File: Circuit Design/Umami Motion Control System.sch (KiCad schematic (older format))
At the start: 7 parts

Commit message: schematic work
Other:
- moved on the sheet: C?, IC?, K?, X?
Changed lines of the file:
@@
 $Descr A4 11693 8268
 encoding utf-8
-Sheet 1 2
+Sheet 1 3
 Title ""
 Date "8 may 2014"
@@
 L ATMEGA328P-P-RESCUE-Umami_Motion_Control_System IC?
 U 1 1 53642346
-P 4700 3900
-F 0 "IC?" H 3950 5150 40  0000 L BNN
-F 1 "ATMEGA328P-P" H 5100 2500 40  0000 L BNN
-F 2 "DIL28" H 4700 3900 30  0000 C CIN
-F 3 "" H 4700 3900 60  0000 C CNN
-	1    4700 3900
+P 13650 4150
+F 0 "IC?" H 12900 5400 40  0000 L BNN
+F 1 "ATMEGA328P-P" H 14050 2750 40  0000 L BNN
+F 2 "DIL28" H 13650 4150 30  0000 C CIN
+F 3 "" H 13650 4150 60  0000 C CNN
+	1    13650 4150
 	1    0    0    -1
 $EndComp
@@
 L CONN_3 K?
 U 1 1 536423A1
-P 7250 1900
-F 0 "K?" V 7200 1900 50  0000 C CNN
-F 1 "CONN_3" V 7300 1900 40  0000 C CNN
-F 2 "" H 7250 1900 60  0000 C CNN
-F 3 "" H 7250 1900 60  0000 C CNN
-	1    7250 1900
+P 16200 2150
+F 0 "K?" V 16150 2150 50  0000 C CNN
+F 1 "CONN_3" V 16250 2150 40  0000 C CNN
+F 2 "" H 16200 2150 60  0000 C CNN
+F 3 "" H 16200 2150 60  0000 C CNN
+	1    16200 2150
 	1    0    0    -1
 $EndComp
@@
 L CRYSTAL X?
 U 1 1 5364240B
-P 7650 3450
-F 0 "X?" H 7650 3600 60  0000 C CNN
-F 1 "CRYSTAL" H 7650 3300 60  0000 C CNN
-F 2 "~" H 7650 3450 60  0000 C CNN
-F 3 "~" H 7650 3450 60  0000 C CNN
-	1    7650 3450
+P 16600 3700
+F 0 "X?" H 16600 3850 60  0000 C CNN
+F 1 "CRYSTAL" H 16600 3550 60  0000 C CNN
+F 2 "~" H 16600 3700 60  0000 C CNN
+F 3 "~" H 16600 3700 60  0000 C CNN
+	1    16600 3700
 	0    1    1    0
 $EndComp
-Text Notes 7400 1800 0    60   ~ 0
+Text Notes 16350 2050 0    60   ~ 0
 pan pot
 $Comp
 L CONN_3 K?
 U 1 1 53642559
-P 7250 2300
-F 0 "K?" V 7200 2300 50  0000 C CNN
-F 1 "CONN_3" V 7300 2300 40  0000 C CNN
-F 2 "" H 7250 2300 60  0000 C CNN
-F 3 "" H 7250 2300 60  0000 C CNN
-	1    7250 2300
+P 16200 2550
+F 0 "K?" V 16150 2550 50  0000 C CNN
+F 1 "CONN_3" V 16250 2550 40  0000 C CNN
+F 2 "" H 16200 2550 60  0000 C CNN
+F 3 "" H 16200 2550 60  0000 C CNN
+	1    16200 2550
 	1    0    0    -1
 $EndComp
-Text Notes 7400 2200 0    60   ~ 0
+Text Notes 16350 2450 0    60   ~ 0
 tilt pot
 $Comp
 L +5V #PWR?
 U 1 1 53642590
-P 4450 1400
-F 0 "#PWR?" H 4450 1490 20  0001 C CNN
-F 1 "+5V" H 4450 1550 30  0000 C CNN
-F 2 "" H 4450 1400 60  0000 C CNN
-F 3 "" H 4450 1400 60  0000 C CNN
-	1    4450 1400
+P 13400 1650
+F 0 "#PWR?" H 13400 1740 20  0001 C CNN
+F 1 "+5V" H 13400 1800 30  0000 C CNN
+F 2 "" H 13400 1650 60  0000 C CNN
+F 3 "" H 13400 1650 60  0000 C CNN
+	1    13400 1650
 	1    0    0    -1
 $EndComp
-Text Notes 7400 2550 0    60   ~ 0
+Text Notes 16350 2800 0    60   ~ 0
 Focus Pot
 $Comp
 L C-RESCUE-Umami_Motion_Control_System C?
 U 1 1 536C0691
-P 7850 3750
-F 0 "C?" H 7850 3850 40  0000 L CNN
-F 1 "C" H 7856 3665 40  0000 L CNN
-F 2 "~" H 7888 3600 30  0000 C CNN
-F 3 "~" H 7850 3750 60  0000 C CNN
-	1    7850 3750
+P 16800 4000
+F 0 "C?" H 16800 4100 40  0000 L CNN
+F 1 "C" H 16806 3915 40  0000 L CNN
+F 2 "~" H 16838 3850 30  0000 C CNN
+F 3 "~" H 16800 4000 60  0000 C CNN
+	1    16800 4000
 	0    -1   -1   0
 $EndComp
@@
 L C-RESCUE-Umami_Motion_Control_System C?
 U 1 1 536C06A8
-P 7850 3150
-F 0 "C?" H 7850 3250 40  0000 L CNN
-F 1 "C" H 7856 3065 40  0000 L CNN
-F 2 "~" H 7888 3000 30  0000 C CNN
-F 3 "~" H 7850 3150 60  0000 C CNN
-	1    7850 3150
+P 16800 3400
+F 0 "C?" H 16800 3500 40  0000 L CNN
+F 1 "C" H 16806 3315 40  0000 L CNN
+F 2 "~" H 16838 3250 30  0000 C CNN
+F 3 "~" H 16800 3400 60  0000 C CNN
+	1    16800 3400
 	0    -1   -1   0
 $EndComp
@@
 L CONN_3 K?
 U 1 1 5364264D
-P 7250 2650
-F 0 "K?" V 7200 2650 50  0000 C CNN
-F 1 "CONN_3" V 7300 2650 40  0000 C CNN
-F 2 "" H 7250 2650 60  0000 C CNN
-F 3 "" H 7250 2650 60  0000 C CNN
-	1    7250 2650
+P 16200 2900
+F 0 "K?" V 16150 2900 50  0000 C CNN
+F 1 "CONN_3" V 16250 2900 40  0000 C CNN
+F 2 "" H 16200 2900 60  0000 C CNN
+F 3 "" H 16200 2900 60  0000 C CNN
+	1    16200 2900
 	1    0    0    -1
 $EndComp
@@
 L GND-RESCUE-Umami_Motion_Control_System #PWR?
 U 1 1 536C0735
-P 8050 5250
-F 0 "#PWR?" H 8050 5250 30  0001 C CNN
-F 1 "GND" H 8050 5180 30  0001 C CNN
-F 2 "" H 8050 5250 60  0000 C CNN
-F 3 "" H 8050 5250 60  0000 C CNN
-	1    8050 5250
+P 17000 5500
+F 0 "#PWR?" H 17000 5500 30  0001 C CNN
+F 1 "GND" H 17000 5430 30  0001 C CNN
+F 2 "" H 17000 5500 60  0000 C CNN
+F 3 "" H 17000 5500 60  0000 C CNN
+	1    17000 5500
 	1    0    0    -1
 $EndComp
 Wire Wire Line
-	6300 3850 5700 3850
+	15250 4100 14650 4100
 Wire Wire Line
-	6300 2650 6300 3850
+	15250 2900 15250 4100
 Wire Wire Line
-	6900 2650 6300 2650
+	15850 2900 15250 2900
 Wire Wire Line
-	6250 3750 5700 3750
+	15200 4000 14650 4000
 Wire Wire Line
-	6250 2300 6250 3750
+	15200 2550 15200 4000
 Wire Wire Line
-	6900 2300 6250 2300
+	15850 2550 15200 2550
 Wire Wire Line
-	6200 3650 5700 3650
+	15150 3900 14650 3900
 Wire Wire Line
-	6200 1900 6200 3650
+	15150 2150 15150 3900
 Wire Wire Line
-	6900 1900 6200 1900
-Connection ~ 4450 1800
+	15850 2150 15150 2150
+Connection ~ 13400 2050
 Wire Wire Line
-	4450 2200 6900 2200
+	13400 2450 15850 2450
 Wire Wire Line
-	4450 1400 4450 2550
+	13400 1650 13400 2800
 Wire Wire Line
-	5700 3500 7400 3500
+	14650 3750 16350 3750
 Wire Wire Line
-	5700 3400 7400 3400
+	14650 3650 16350 3650
 Wire Wire Line
-	7400 3400 7400 3150
+	16350 3650 16350 3400
 Wire Wire Line
-	7400 3150 7650 3150
+	16350 3400 16600 3400
 Wire Wire Line
-	7400 3500 7400 3750
+	16350 3750 16350 4000
 Wire Wire Line
-	7400 3750 7650 3750
+	16350 4000 16600 4000
 Wire Wire Line
-	8050 2900 8050 3750
+	17000 3150 17000 4000
 Wire Wire Line
-	8050 3800 8050 5250
+	17000 4050 17000 5500
 Wire Wire Line
-	6900 2000 6700 2000
+	15850 2250 15650 2250
 Wire Wire Line
-	6700 2000 6700 2900
+	15650 2250 15650 3150
 Wire Wire Line
-	6700 2900 8050 2900
-Connection ~ 8050 3150
+	15650 3150 17000 3150
+Connection ~ 17000 3400
 Wire Wire Line
-	6900 2400 6700 2400
-Connection ~ 6700 2400
+	15850 2650 15650 2650
+Connection ~ 15650 2650
 Wire Wire Line
-	6900 2750 6700 2750
-Connection ~ 6700 2750
+	15850 3000 15650 3000
+Connection ~ 15650 3000
 Wire Wire Line
-	3800 1800 6900 1800
+	12750 2050 15850 2050
 Wire Wire Line
-	4450 2550 6900 2550
-Connection ~ 4450 2200
+	13400 2800 15850 2800
+Connection ~ 13400 2450
 Wire Wire Line
-	3800 1800 3800 2800
+	12750 2050 12750 3050
 $Sheet
 S 1250 1100 900  550
@@
 F1 "Raspi.sch" 60
 $EndSheet
+$Sheet
+S 1200 2900 1150 1150
+U 565B4BE2
+F0 "old work" 60
+F1 "oldwork.sch" 60
+$EndSheet
 $EndSCHEMATC

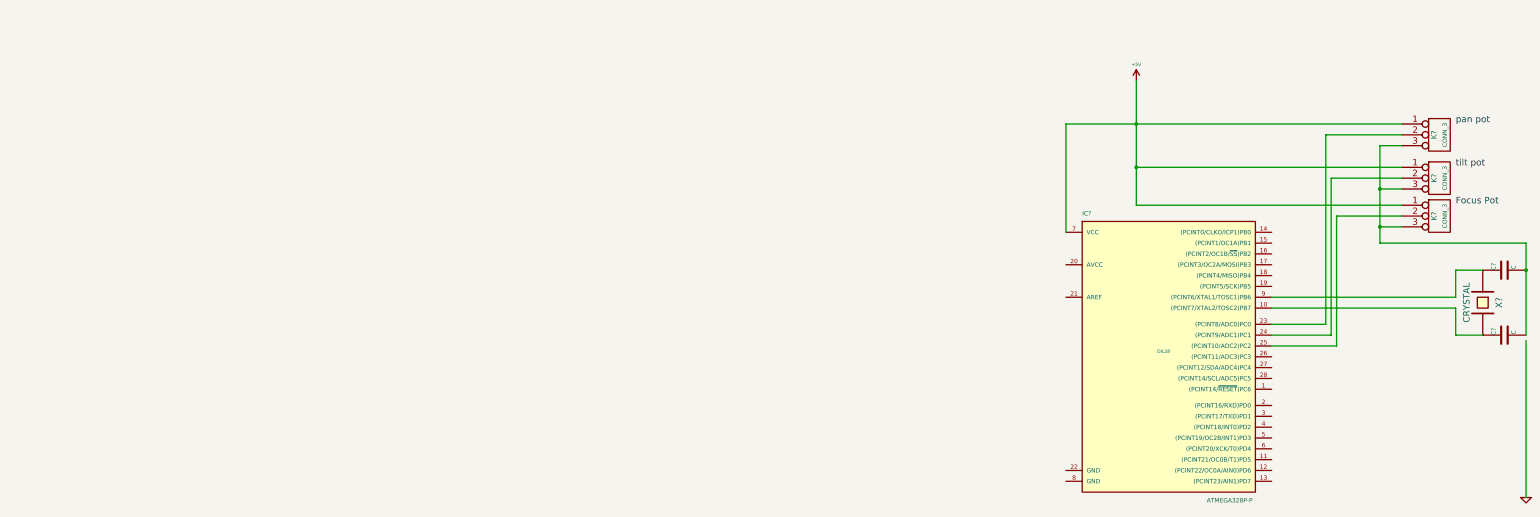
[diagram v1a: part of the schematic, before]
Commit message: socket io working, able to toggle led with phone
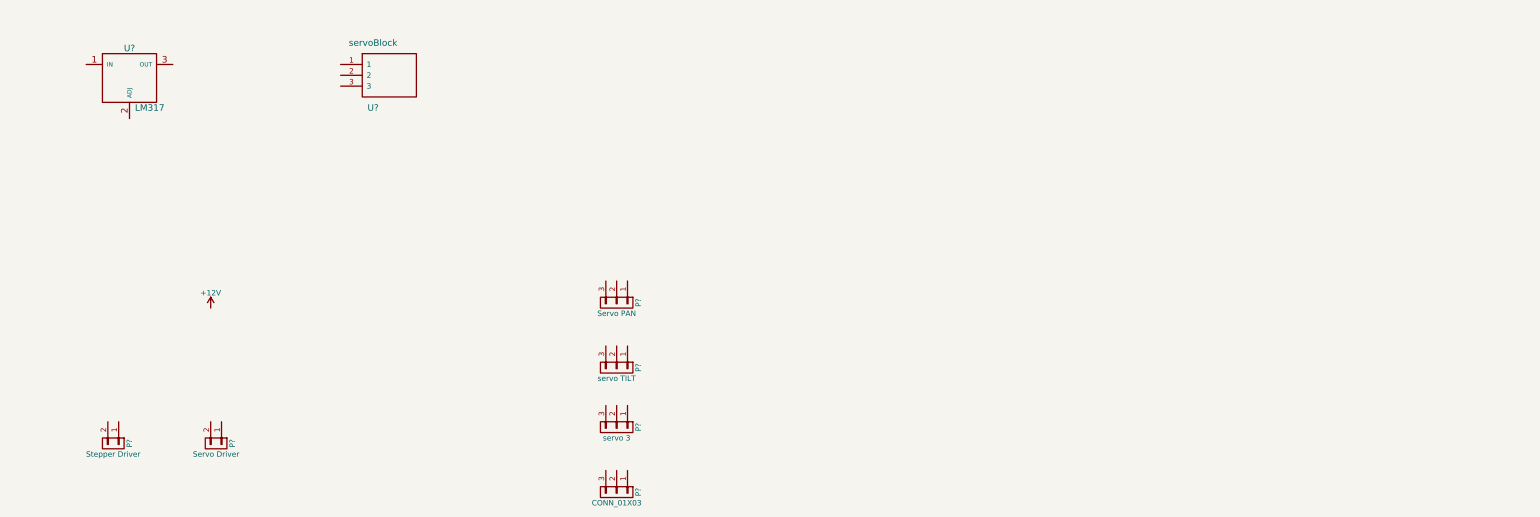
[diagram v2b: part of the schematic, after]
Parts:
- removed C? (x2): C, ~, symbol C-RESCUE-Umami_Motion_Control_System
- removed IC?: ATMEGA328P-P, DIL28, symbol ATMEGA328P-P-RESCUE-Umami_Motion_Control_System
- removed K? (x3): CONN_3, symbol CONN_3
- removed X?: CRYSTAL, ~, symbol CRYSTAL
- added P?: Servo PAN, symbol CONN_01X03
- added P?: servo TILT, symbol CONN_01X03
- added P?: servo 3, symbol CONN_01X03
- added P?: CONN_01X03, symbol CONN_01X03
- added P?: Servo Driver, symbol CONN_01X02
- added P?: Stepper Driver, symbol CONN_01X02
- added U?: LM317, symbol LM317
- added U?: servoBlock, symbol servoBlock
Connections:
- net labels added: +12V
- net labels removed: +5V, GND
- wire segments 27 -> 0
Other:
- note removed: "Focus Pot"
- note removed: "pan pot"
- note removed: "tilt pot"
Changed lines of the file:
@@
 Comment4 ""
 $EndDescr
-$Comp
-L ATMEGA328P-P-RESCUE-Umami_Motion_Control_System IC?
-U 1 1 53642346
-P 13650 4150
-F 0 "IC?" H 12900 5400 40  0000 L BNN
-F 1 "ATMEGA328P-P" H 14050 2750 40  0000 L BNN
-F 2 "DIL28" H 13650 4150 30  0000 C CIN
-F 3 "" H 13650 4150 60  0000 C CNN
-	1    13650 4150
-	1    0    0    -1
-$EndComp
-$Comp
-L CONN_3 K?
-U 1 1 536423A1
-P 16200 2150
-F 0 "K?" V 16150 2150 50  0000 C CNN
-F 1 "CONN_3" V 16250 2150 40  0000 C CNN
-F 2 "" H 16200 2150 60  0000 C CNN
-F 3 "" H 16200 2150 60  0000 C CNN
-	1    16200 2150
-	1    0    0    -1
-$EndComp
-$Comp
-L CRYSTAL X?
-U 1 1 5364240B
-P 16600 3700
-F 0 "X?" H 16600 3850 60  0000 C CNN
-F 1 "CRYSTAL" H 16600 3550 60  0000 C CNN
-F 2 "~" H 16600 3700 60  0000 C CNN
-F 3 "~" H 16600 3700 60  0000 C CNN
-	1    16600 3700
-	0    1    1    0
-$EndComp
-Text Notes 16350 2050 0    60   ~ 0
-pan pot
-$Comp
-L CONN_3 K?
-U 1 1 53642559
-P 16200 2550
-F 0 "K?" V 16150 2550 50  0000 C CNN
-F 1 "CONN_3" V 16250 2550 40  0000 C CNN
-F 2 "" H 16200 2550 60  0000 C CNN
-F 3 "" H 16200 2550 60  0000 C CNN
-	1    16200 2550
-	1    0    0    -1
-$EndComp
-Text Notes 16350 2450 0    60   ~ 0
-tilt pot
-$Comp
-L +5V #PWR?
-U 1 1 53642590
-P 13400 1650
-F 0 "#PWR?" H 13400 1740 20  0001 C CNN
-F 1 "+5V" H 13400 1800 30  0000 C CNN
-F 2 "" H 13400 1650 60  0000 C CNN
-F 3 "" H 13400 1650 60  0000 C CNN
-	1    13400 1650
-	1    0    0    -1
-$EndComp
-Text Notes 16350 2800 0    60   ~ 0
-Focus Pot
-$Comp
-L C-RESCUE-Umami_Motion_Control_System C?
-U 1 1 536C0691
-P 16800 4000
-F 0 "C?" H 16800 4100 40  0000 L CNN
-F 1 "C" H 16806 3915 40  0000 L CNN
-F 2 "~" H 16838 3850 30  0000 C CNN
-F 3 "~" H 16800 4000 60  0000 C CNN
-	1    16800 4000
-	0    -1   -1   0
-$EndComp
-$Comp
-L C-RESCUE-Umami_Motion_Control_System C?
-U 1 1 536C06A8
-P 16800 3400
-F 0 "C?" H 16800 3500 40  0000 L CNN
-F 1 "C" H 16806 3315 40  0000 L CNN
-F 2 "~" H 16838 3250 30  0000 C CNN
-F 3 "~" H 16800 3400 60  0000 C CNN
-	1    16800 3400
-	0    -1   -1   0
-$EndComp
-$Comp
-L CONN_3 K?
-U 1 1 5364264D
-P 16200 2900
-F 0 "K?" V 16150 2900 50  0000 C CNN
-F 1 "CONN_3" V 16250 2900 40  0000 C CNN
-F 2 "" H 16200 2900 60  0000 C CNN
-F 3 "" H 16200 2900 60  0000 C CNN
-	1    16200 2900
-	1    0    0    -1
-$EndComp
-$Comp
-L GND-RESCUE-Umami_Motion_Control_System #PWR?
-U 1 1 536C0735
-P 17000 5500
-F 0 "#PWR?" H 17000 5500 30  0001 C CNN
-F 1 "GND" H 17000 5430 30  0001 C CNN
-F 2 "" H 17000 5500 60  0000 C CNN
-F 3 "" H 17000 5500 60  0000 C CNN
-	1    17000 5500
-	1    0    0    -1
-$EndComp
-Wire Wire Line
-	15250 4100 14650 4100
-Wire Wire Line
-	15250 2900 15250 4100
-Wire Wire Line
-	15850 2900 15250 2900
-Wire Wire Line
-	15200 4000 14650 4000
-Wire Wire Line
-	15200 2550 15200 4000
-Wire Wire Line
-	15850 2550 15200 2550
-Wire Wire Line
-	15150 3900 14650 3900
-Wire Wire Line
-	15150 2150 15150 3900
-Wire Wire Line
-	15850 2150 15150 2150
-Connection ~ 13400 2050
-Wire Wire Line
-	13400 2450 15850 2450
-Wire Wire Line
-	13400 1650 13400 2800
-Wire Wire Line
-	14650 3750 16350 3750
-Wire Wire Line
-	14650 3650 16350 3650
-Wire Wire Line
-	16350 3650 16350 3400
-Wire Wire Line
-	16350 3400 16600 3400
-Wire Wire Line
-	16350 3750 16350 4000
-Wire Wire Line
-	16350 4000 16600 4000
-Wire Wire Line
-	17000 3150 17000 4000
-Wire Wire Line
-	17000 4050 17000 5500
-Wire Wire Line
-	15850 2250 15650 2250
-Wire Wire Line
-	15650 2250 15650 3150
-Wire Wire Line
-	15650 3150 17000 3150
-Connection ~ 17000 3400
-Wire Wire Line
-	15850 2650 15650 2650
-Connection ~ 15650 2650
-Wire Wire Line
-	15850 3000 15650 3000
-Connection ~ 15650 3000
-Wire Wire Line
-	12750 2050 15850 2050
-Wire Wire Line
-	13400 2800 15850 2800
-Connection ~ 13400 2450
-Wire Wire Line
-	12750 2050 12750 3050
 $Sheet
 S 1250 1100 900  550
@@
 F1 "oldwork.sch" 60
 $EndSheet
+$Comp
+L LM317 U?
+U 1 1 565B5C82
+P 4100 1650
+F 0 "U?" H 4100 1950 60  0000 C CNN
+F 1 "LM317" H 4150 1400 60  0000 L CNN
+F 2 "" H 4100 1650 60  0000 C CNN
+F 3 "" H 4100 1650 60  0000 C CNN
+	1    4100 1650
+	1    0    0    -1
+$EndComp
+$Comp
+L servoBlock U?
+U 1 1 565B76FD
+P 6350 1400
+F 0 "U?" H 6350 900 60  0000 C CNN
+F 1 "servoBlock" H 6350 1500 60  0000 C CNN
+F 2 "" H 6050 1400 60  0000 C CNN
+F 3 "" H 6050 1400 60  0000 C CNN
+	1    6350 1400
+	1    0    0    -1
+$EndComp
+$Comp
+L CONN_01X03 P?
+U 1 1 565B7937
+P 8600 3700
+F 0 "P?" H 8600 3900 50  0000 C CNN
+F 1 "Servo PAN" V 8700 3700 50  0000 C CNN
+F 2 "" H 8600 3700 60  0000 C CNN
+F 3 "" H 8600 3700 60  0000 C CNN
+	1    8600 3700
+	0    1    1    0
+$EndComp
+$Comp
+L CONN_01X03 P?
+U 1 1 565B79D8
+P 8600 4300
+F 0 "P?" H 8600 4500 50  0000 C CNN
+F 1 "servo TILT" V 8700 4300 50  0000 C CNN
+F 2 "" H 8600 4300 60  0000 C CNN
+F 3 "" H 8600 4300 60  0000 C CNN
+	1    8600 4300
+	0    1    1    0
+$EndComp
+$Comp
+L CONN_01X03 P?
+U 1 1 565B7A79
+P 8600 4850
+F 0 "P?" H 8600 5050 50  0000 C CNN
+F 1 "servo 3" V 8700 4850 50  0000 C CNN
+F 2 "" H 8600 4850 60  0000 C CNN
+F 3 "" H 8600 4850 60  0000 C CNN
+	1    8600 4850
+	0    1    1    0
+$EndComp
+$Comp
+L CONN_01X03 P?
+U 1 1 565B7AAE
+P 8600 5450
+F 0 "P?" H 8600 5650 50  0000 C CNN
+F 1 "CONN_01X03" V 8700 5450 50  0000 C CNN
+F 2 "" H 8600 5450 60  0000 C CNN
+F 3 "" H 8600 5450 60  0000 C CNN
+	1    8600 5450
+	0    1    1    0
+$EndComp
+$Comp
+L CONN_01X02 P?
+U 1 1 565B7EFB
+P 4900 5000
+F 0 "P?" H 4900 5150 50  0000 C CNN
+F 1 "Servo Driver" V 5000 5000 50  0000 C CNN
+F 2 "" H 4900 5000 60  0000 C CNN
+F 3 "" H 4900 5000 60  0000 C CNN
+	1    4900 5000
+	0    1    1    0
+$EndComp
+$Comp
+L CONN_01X02 P?
+U 1 1 565B80D2
+P 3950 5000
+F 0 "P?" H 3950 5150 50  0000 C CNN
+F 1 "Stepper Driver" V 4050 5000 50  0000 C CNN
+F 2 "" H 3950 5000 60  0000 C CNN
+F 3 "" H 3950 5000 60  0000 C CNN
+	1    3950 5000
+	0    1    1    0
+$EndComp
+$Comp
+L +12V #PWR?
+U 1 1 565B81E7
+P 4850 3750
+F 0 "#PWR?" H 4850 3600 50  0001 C CNN
+F 1 "+12V" H 4850 3890 50  0000 C CNN
+F 2 "" H 4850 3750 60  0000 C CNN
+F 3 "" H 4850 3750 60  0000 C CNN
+	1    4850 3750
+	1    0    0    -1
+$EndComp
 $EndSCHEMATC
